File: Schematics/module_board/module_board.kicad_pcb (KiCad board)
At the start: 2 copper layers, 17 parts, among them U1 RP2040, U3 LSM6DS3

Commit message: Updated Footprints, started PCB design
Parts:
- removed C15: C, Capacitor_SMD:C_0402_1005Metric
- removed U3: LSM6DS3, Package_LGA:LGA-14_3x2.5mm_P0.5mm_LayoutBorder3x4y
- added J1: Conn_01x01_Male, TestPoint:TestPoint_Pad_D2.0mm, F.Cu at (146.8, 88.0)
- added J10: Conn_01x01_Male, TestPoint:TestPoint_Plated_Hole_D2.0mm, F.Cu at (167.3, 101.2)
- added J2: Conn_01x01_Male, TestPoint:TestPoint_Pad_D2.0mm, F.Cu at (150.8, 84.0)
- added J3: Conn_01x01_Male, TestPoint:TestPoint_Pad_D2.0mm, F.Cu at (146.8, 84.0)
- added J4: Conn_01x01_Male, TestPoint:TestPoint_Pad_D2.0mm, F.Cu at (150.8, 88.0)
- added J5: Conn_01x01_Male, TestPoint:TestPoint_Plated_Hole_D2.0mm, F.Cu at (171.9, 96.6)
- added J6: Conn_01x01_Male, TestPoint:TestPoint_Plated_Hole_D2.0mm, F.Cu at (162.7, 101.2)
- added J7: Conn_01x01_Male, TestPoint:TestPoint_Plated_Hole_D2.0mm, F.Cu at (167.3, 96.6)
- added J8: Conn_01x01_Male, TestPoint:TestPoint_Plated_Hole_D2.0mm, F.Cu at (171.9, 101.2)
- added J9: Conn_01x01_Male, TestPoint:TestPoint_Plated_Hole_D2.0mm, F.Cu at (162.7, 96.6)
- added R5: 10k, Resistor_SMD:R_0402_1005Metric, F.Cu at (143.9, 75.5)
- added R8: 10k, Resistor_SMD:R_0402_1005Metric, F.Cu at (144.0, 72.5)
- added R9: 1k, Resistor_SMD:R_0402_1005Metric, F.Cu at (171.1, 79.4)
- added U2: W25Q16JVSSIQ, W25Q16JVSSIQ:SOIC127P790X216-8N, F.Cu at (150.4, 73.9)
- added Y1: ABLS-12.000MHZ-B4-T, ABLS-12:XTAL_ABLS-12.000MHZ-B4-T, F.Cu at (164.8, 73.6)
- C10: value 100nF -> 100n
- C3, C4: footprint Capacitor_SMD:C_0603_1608Metric -> Capacitor_SMD:C_0402_1005Metric
- C7, C8: value 10pF -> 27p
- moved C8 62.9 mm to (168.4, 80.6)
- moved C7 57.0 mm to (168.7, 78.4)
- moved C4 53.2 mm to (160.2, 80.1), turned to 90 degrees
- moved C3 52.9 mm to (158.8, 80.1), turned to 90 degrees
- moved U1 49.0 mm to (158.2, 85.6)
- moved C10 42.8 mm to (141.6, 74.0)
- moved C6 26.6 mm to (142.2, 100.3)
- moved C9 25.3 mm to (142.1, 97.6)
- moved C5 25.0 mm to (142.3, 103.0)
- moved C2 24.6 mm to (144.9, 93.1)
- moved C14 22.4 mm to (148.5, 100.3)
- moved C12 22.3 mm to (145.0, 100.2)
- moved C13 22.2 mm to (145.0, 103.0)
- moved C11 18.2 mm to (145.0, 97.5)
- moved C1 17.4 mm to (142.5, 92.9)
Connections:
- C7 pad 2: Net-(C7-Pad2) -> /XTAL_IN
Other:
- board outline added: 35 x 35 mm

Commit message: Completed non-routed Rough PCB Draft
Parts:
- added J11: Conn_01x01_Male, TestPoint:TestPoint_Plated_Hole_D2.0mm, F.Cu at (147.0, 101.1)
- added J12: Conn_01x01_Male, TestPoint:TestPoint_Plated_Hole_D2.0mm, F.Cu at (147.1, 97.0)
- added J13: Conn_01x01_Male, TestPoint:TestPoint_Plated_Hole_D2.0mm, F.Cu at (157.6, 96.5)
- added J14: Conn_01x01_Male, TestPoint:TestPoint_Plated_Hole_D2.0mm, F.Cu at (154.2, 94.0)
- added J15: Conn_01x01_Male, TestPoint:TestPoint_Plated_Hole_D2.0mm, F.Cu at (147.1, 92.9)
- added J16: Conn_01x01_Male, TestPoint:TestPoint_Plated_Hole_D2.0mm, F.Cu at (147.2, 89.3)
- added J17: Conn_01x01_Male, TestPoint:TestPoint_Plated_Hole_D2.0mm, F.Cu at (147.2, 85.6)
- added JP1: Jumper_2_Open, Jumper:SolderJumper-2_P1.3mm_Open_Pad1.0x1.5mm, F.Cu at (148.1, 81.2)
- U2: footprint W25Q16JVSSIQ:SOIC127P790X216-8N -> Package_SO:SOIC-8_5.23x5.23mm_P1.27mm
- moved J10 37.5 mm to (169.8, 63.9)
- moved J8 37.5 mm to (174.4, 63.9)
- moved J5 37.5 mm to (174.4, 59.2)
- moved J7 37.5 mm to (169.8, 59.2)
- moved J6 33.0 mm to (169.7, 69.0)
- moved J9 30.7 mm to (174.5, 68.3)
- moved C5 30.6 mm to (166.3, 84.0), turned to 90 degrees
- moved Y1 29.6 mm to (156.8, 102.1)
- moved J3 28.2 mm to (167.6, 103.1)
- moved C6 26.3 mm to (162.9, 84.0), turned to 90 degrees
- moved R9 25.4 mm to (153.6, 97.8), turned to 90 degrees
- moved C8 24.6 mm to (150.9, 97.8), turned to -90 degrees
- moved C12 23.5 mm to (166.4, 90.6)
- moved J2 23.0 mm to (167.6, 99.8)
- moved J1 22.5 mm to (167.7, 96.5)
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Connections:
- C3 pad 1: +1V1 -> GND
- C3 pad 2: GND -> +1V1
- U1 pad 11: /GPIO8 -> /SPI1_RX
- U1 pad 12: /GPIO9 -> /SPI1_CS_IO9
- U1 pad 13: /GPIO10 -> /SPI1_SCK
- U1 pad 14: /GPIO11 -> /SPI1_TX
- U1 pad 27: /GPIO16 -> /RX
- U1 pad 28: /GPIO17 -> /CS
- U1 pad 29: /GPIO18 -> /SCLK
- U1 pad 30: /GPIO19 -> /TX
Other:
- board size 35 x 35 mm -> 30 x 30 mm

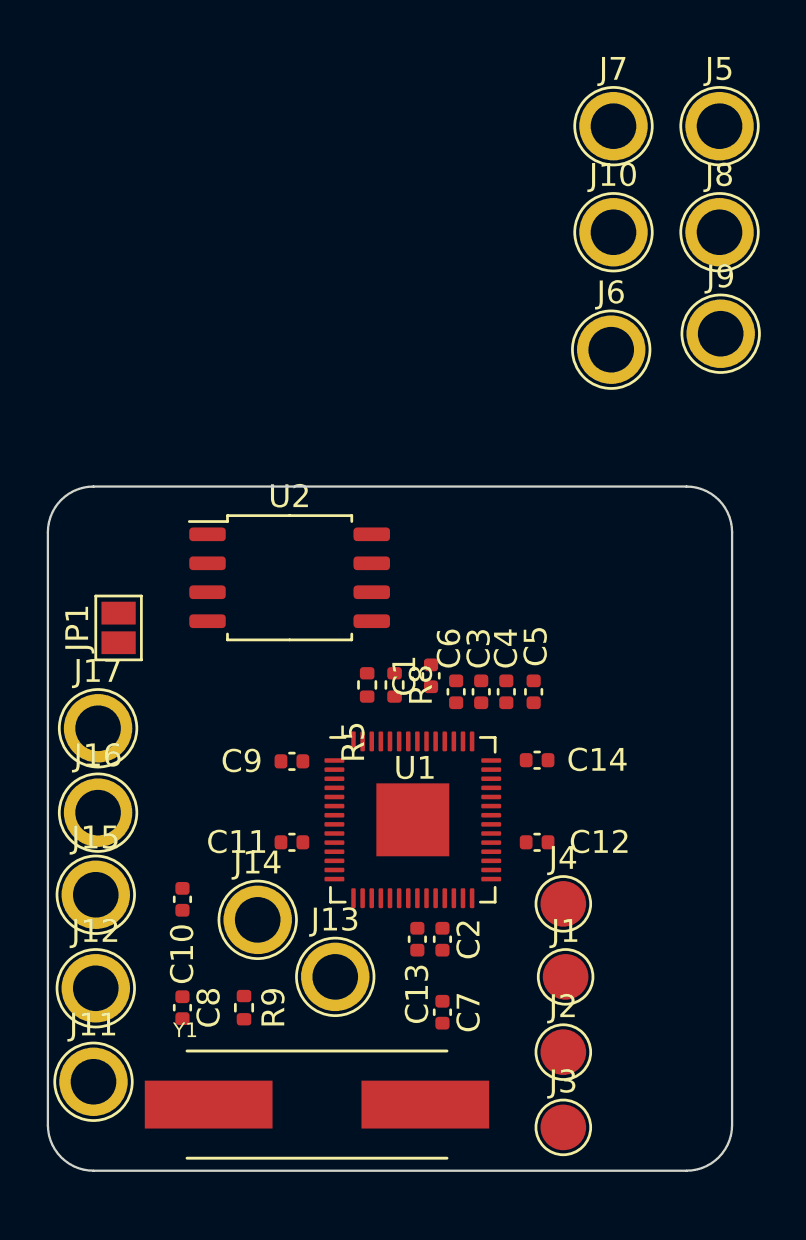
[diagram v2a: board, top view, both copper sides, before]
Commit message: Completed PCB Routing, Reassigned Pins, Assigned Pogo Footprint
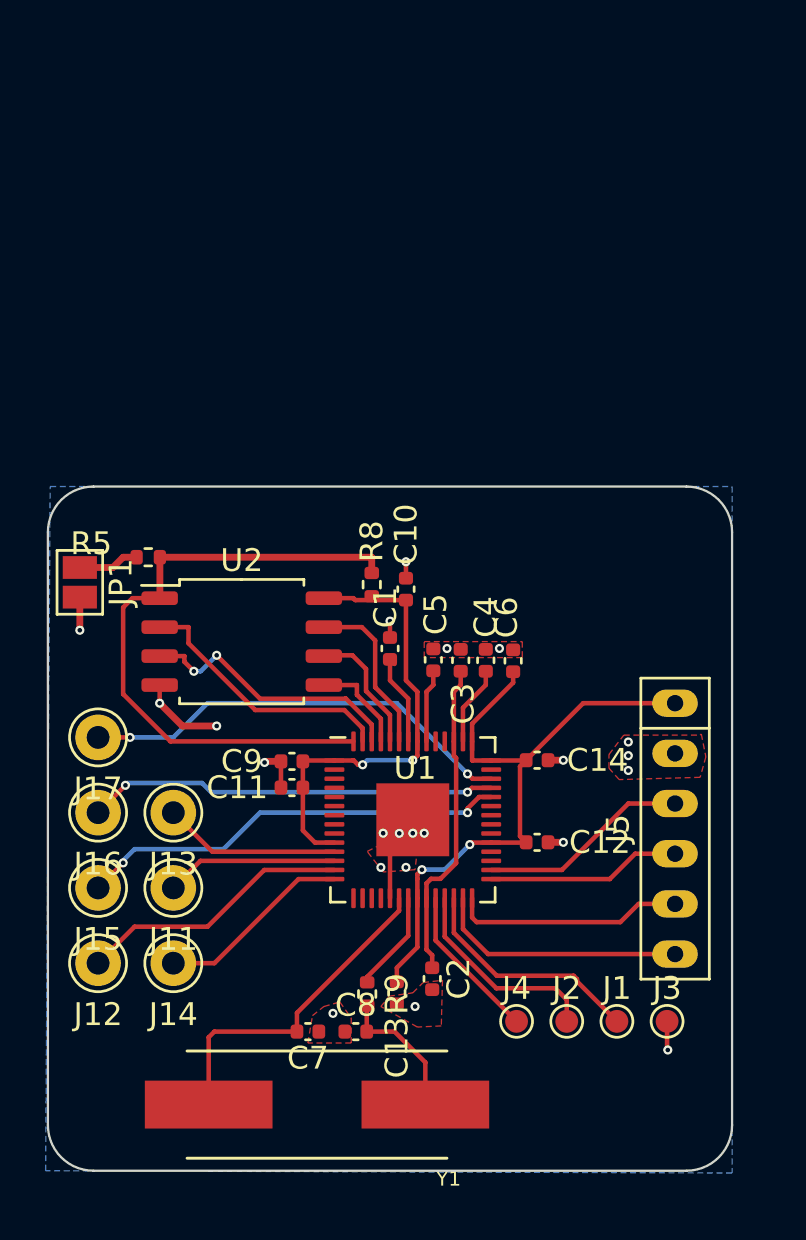
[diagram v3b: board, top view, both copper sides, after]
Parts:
- removed J10, J6, J7, J8, J9: Conn_01x01_Male, TestPoint:TestPoint_Plated_Hole_D2.0mm
- J1, J2, J3, J4: footprint TestPoint:TestPoint_Pad_D2.0mm -> TestPoint:TestPoint_Pad_D1.0mm
- J11, J12, J13, J14, J15, J16, J17: footprint TestPoint:TestPoint_Plated_Hole_D2.0mm -> Connector_Pin:Pin_D1.0mm_L10.0mm
- J5: value Conn_01x01_Male -> Conn_01x06_Male; footprint TestPoint:TestPoint_Plated_Hole_D2.0mm -> Prototroller:Mag_Pogo_6P_P2.2mm_Male
- moved J5 30.9 mm to (172.5, 90.0), turned to -90 degrees
- moved C10 16.8 mm to (160.7, 79.5), turned to 90 degrees
- moved R5 11.1 mm to (149.4, 78.1), turned to 0 degrees
- moved J13 10.1 mm to (150.5, 89.3)
- moved J11 9.19 mm to (150.5, 92.6)
- moved C8 7.67 mm to (158.5, 98.9), turned to 0 degrees
- moved J3 6.51 mm to (172.2, 98.5)
- moved C7 5.96 mm to (156.4, 98.9), turned to 180 degrees
- moved J4 5.54 mm to (165.6, 98.5)
- moved R9 5.43 mm to (159.0, 97.2)
- moved C5 4.62 mm to (161.9, 82.6)
- moved R8 4.51 mm to (159.2, 79.3)
- moved J14 4.16 mm to (150.5, 95.9)
- moved U2 3.50 mm to (153.5, 81.8)
- moved J1 2.98 mm to (169.9, 98.5)
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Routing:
- net +3V3: track 0.00 -> 56.1 mm, vias 0 -> 4
- net /QSPI_NSS: track 0.00 -> 28.3 mm
- net /GPIO28_ADC2: track 0.00 -> 19.2 mm, vias 0 -> 2
- net /GPIO26_ADC0: track 0.00 -> 19.1 mm, vias 0 -> 2
- net +1V1: track 0.00 -> 18.3 mm
- net /GPIO27_ADC1: track 0.00 -> 18.0 mm, vias 0 -> 2
- net GND: track 0.00 -> 15.0 mm, vias 0 -> 22
- net /XTAL_IN: track 0.00 -> 14.6 mm
- net /SPI1_SCK: track 0.00 -> 12.1 mm
- net /QSPI_SD2: track 0.00 -> 12.0 mm, vias 0 -> 2
- net /QSPI_SD1: track 0.00 -> 11.8 mm
- net /RX: track 0.00 -> 11.1 mm
- net /RESET_N: track 0.00 -> 10.3 mm
- net /CS: track 0.00 -> 10.2 mm
- net /TX: track 0.00 -> 9.27 mm
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- added copper zone on B.Cu, net GND
- added copper zone on F.Cu, net GND
